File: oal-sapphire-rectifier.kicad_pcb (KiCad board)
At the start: 2 copper layers, 100 x 80 mm, 0 parts

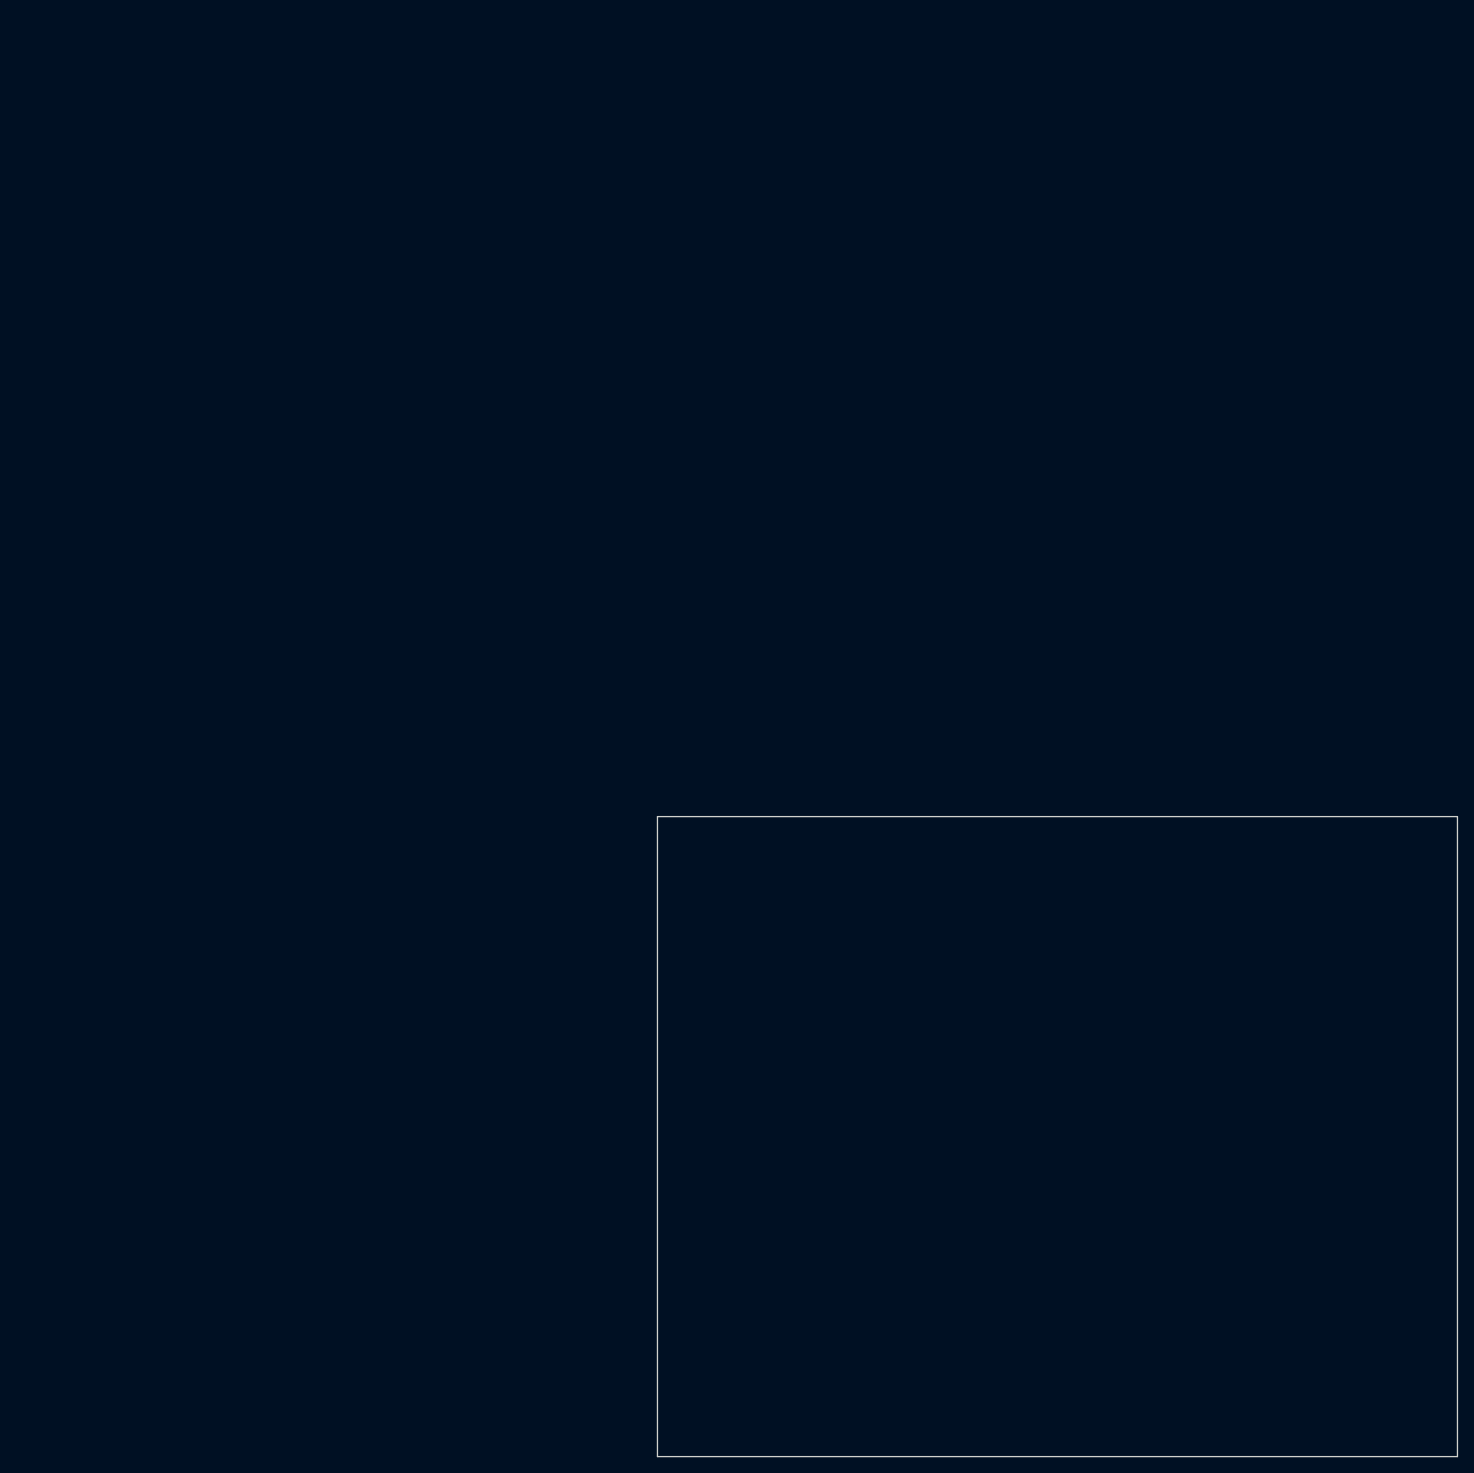
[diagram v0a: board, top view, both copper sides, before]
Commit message: initial component placement
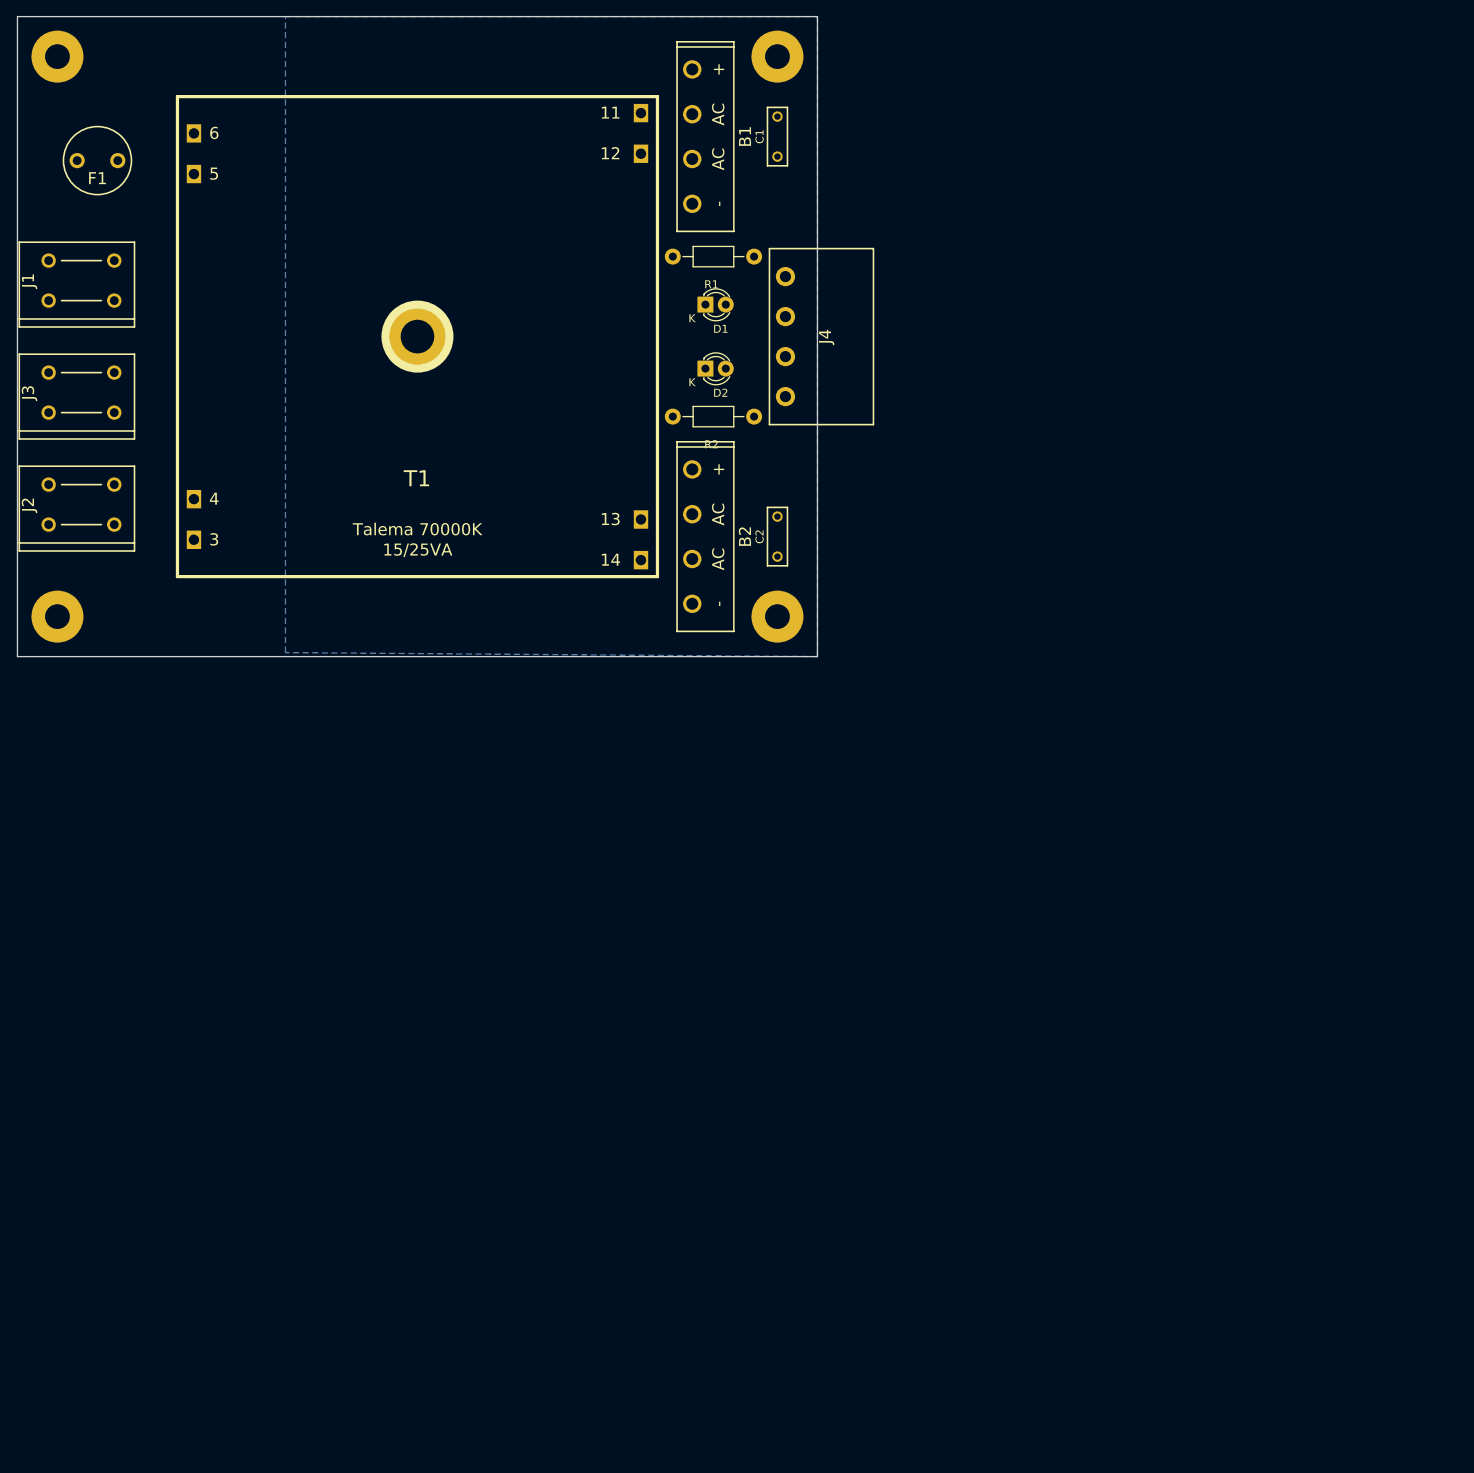
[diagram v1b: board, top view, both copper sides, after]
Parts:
- added B1: KBU4, ose-audio-labs:VISHAY-KBU4, F.Cu at (86.0, -25.0)
- added B2: KBU4, ose-audio-labs:VISHAY-KBU4, F.Cu at (86.0, 25.0)
- added C1: 0.1uF, ose-audio-labs:TDK-B32529-63VAC, F.Cu at (95.0, -25.0)
- added C2: 0.1uF, ose-audio-labs:TDK-B32529-63VAC, F.Cu at (95.0, 25.0)
- added D1: LED, LEDs:LED-3MM, F.Cu at (86.0, -4.00)
- added D2: LED, LEDs:LED-3MM, F.Cu at (86.0, 4.00)
- added F1: FUSE, ose-audio-labs:LITTLEFUSE-560-TR5, F.Cu at (10.0, -22.0)
- added J1: LINE, ose-audio-labs:PHEONIX_SPT_5-2POS, F.Cu at (8.00, -7.00)
- added J2: NEUTRAL, ose-audio-labs:PHEONIX_SPT_5-2POS, F.Cu at (8.00, 21.0)
- added J3: GROUND, ose-audio-labs:PHEONIX_SPT_5-2POS, F.Cu at (8.00, 7.00)
- added J4: OUTPUT, ose-audio-labs:MSTBA-2.5_4-G, F.Cu at (96.0, 0.00)
- added R1: 820R, Resistors_ThroughHole:Resistor_Horizontal_RM10mm, F.Cu at (87.0, -10.0)
- added R2: 820R, Resistors_ThroughHole:Resistor_Horizontal_RM10mm, F.Cu at (87.0, 10.0)
- added T1: TALEMA-25VA/12V, ose-audio-labs:TALEMA_70000K_15-25VA, F.Cu at (50.0, 0.00)
- added X1: MOUNTING_HOLE, ose-audio-labs:MOUNTING_HOLE-M3, F.Cu at (5.00, 35.0)
- added X2: MOUNTING_HOLE, ose-audio-labs:MOUNTING_HOLE-M3, F.Cu at (95.0, 35.0)
- added X3: MOUNTING_HOLE, ose-audio-labs:MOUNTING_HOLE-M3, F.Cu at (5.00, -35.0)
- added X4: MOUNTING_HOLE, ose-audio-labs:MOUNTING_HOLE-M3, F.Cu at (95.0, -35.0)
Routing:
- added copper zone on B.Cu, net GROUND
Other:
- net class Default: clearance 0.2 -> 0.65; trace_width 0.25 -> 1.2
- net class MAINS added: clearance 1.2, trace_width 1.5, via_dia 0.6, via_drill 0.4
- rule trace_clearance: 0.2 -> 0.65

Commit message: initial layout
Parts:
- D1, D2: footprint LEDs:LED-3MM -> LEDs:LED-5MM
- J4: footprint ose-audio-labs:MSTBA-2.5_4-G -> MSTBA-2.5_4-G
- T1: footprint ose-audio-labs:TALEMA_70000K_15-25VA -> TALEMA_70000K_15-25VA
- moved J2 14.0 mm to (8.00, 7.00)
- moved J3 14.0 mm to (8.00, 21.0)
- moved C1 1.00 mm to (95.0, -26.0)
- moved C2 1.00 mm to (95.0, 26.0)
- moved D1 1.00 mm to (86.0, -5.00)
- moved D2 1.00 mm to (86.0, 5.00)
- moved R1 1.00 mm to (87.0, -11.0)
- moved R2 1.00 mm to (87.0, 11.0)
- moved B1 0.75 mm to (86.0, -25.8)
- moved B2 0.75 mm to (86.0, 25.8)
- moved J4 0.50 mm to (96.5, 0.00)
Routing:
- net 120V-NEUTRAL: track 0.00 -> 77.1 mm
- net Net-(F1-Pad2): track 0.00 -> 63.3 mm
- net GROUND: track 0.00 -> 56.0 mm
- net 120V-LINE: track 0.00 -> 40.4 mm
- net V++: track 0.00 -> 29.3 mm
- net Net-(B1-Pad3): track 0.00 -> 17.5 mm
- net Net-(B2-Pad2): track 0.00 -> 17.3 mm
- net Net-(B1-Pad2): track 0.00 -> 17.3 mm
- net Net-(B2-Pad3): track 0.00 -> 17.3 mm
- net V--: track 0.00 -> 16.2 mm
- net Net-(D2-Pad1): track 0.00 -> 7.69 mm
- net Net-(D1-Pad1): track 0.00 -> 7.69 mm
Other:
- net class Default: trace_width 1.2 -> 1.5
- net class MAINS: clearance 1.2 -> 2; trace_width 1.5 -> 2
- board text added: "G"
- board text added: "GND"
- board text added: "L"
- board text added: "N"
- board text added: "Ose Audio Labs 2016 Sapphire Rectifier Rev. A"
- board text added: "V++"
- board text added: "V--"
